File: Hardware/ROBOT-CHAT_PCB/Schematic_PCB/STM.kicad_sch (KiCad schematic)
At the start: 28 parts, among them J2 Conn_02x07_Odd_Even, J3 Conn_01x02, J4 Conn_01x02, SW1 SW_Push_Dual, U1 STM32WB55CEUx, Y1 32MHz

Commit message: Merge PCB v3
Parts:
- removed J2: Conn_02x07_Odd_Even, symbol Connector_Generic:Conn_02x07_Odd_Even
- removed Y1: 32MHz, XRCGB32M000F2P01R0:XRCGB32M000F2P01R0, symbol Device:Crystal_GND24_Small
- added J1: Conn_01x04, Connector_JST:JST_XH_B4B-XH-AM_1x04_P2.50mm_Vertical, symbol Connector_Generic:Conn_01x04
- added J201: Conn_ST_STDC14, Connector_PinHeader_1.27mm:PinHeader_2x07_P1.27mm_Vertical_SMD, symbol Connector:Conn_ST_STDC14
- added Y2: 32MHz, XRCGB32M000F2P01R0:XRCGB32M000F2P01R0, symbol Device:Crystal_GND24_Small
- added Y201: Crystal_Small, ABS07AIG-32.768KHZ-6-D-T:ABS07AIG-32.768KHZ-6-D-T, symbol Device:Crystal_Small
- C10, C13, C4, C5, C6, C7, C8: value 100nF -> 100n; footprint (none) -> Capacitor_SMD:C_0402_1005Metric
- C11, C15, C16, C3, C9: footprint (none) -> Capacitor_SMD:C_0603_1608Metric
- C12, C14, C17, C18: footprint (none) -> Capacitor_SMD:C_0402_1005Metric
- D1: footprint (none) -> LED_SMD:LED_0603_1608Metric
- J3, J4: footprint (none) -> Connector_JST:JST_PH_B2B-PH-K_1x02_P2.00mm_Vertical
- L1, L2: footprint (none) -> Inductor_SMD:L_0603_1608Metric
- R4, R5, R6: footprint (none) -> Resistor_SMD:R_0402_1005Metric
- SW1: footprint Button_Switch_SMD2:SW_Push_1P1T_NO_6x6mm_H9.5mm -> SW_Push_1P1T_NO_6x6mm_H9.5mm:SW_Push_1P1T_NO_6x6mm_H9.5mm
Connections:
- net +3.3V: now also C8.1, U1.40 (VDDUSB), J201.3 (VCC)
- net +5V: now also J1.4 (Pin_4); no longer C8.1, U1.40 (VDDUSB)
- net GND: now also J1.1 (Pin_1), J1.2 (Pin_2), J201.11 (GNDDetect), J201.5 (GND), J201.7 (GND), Y2.2, Y2.4
- net NRST: now also J201.12 (~{RST})
- net STATUS_LEDR: now also U1.13 (PA4); no longer U1.47 (PB7)
- net STATUS_LEDV: now also U1.12 (PA3); no longer U1.46 (PB6)
- net SWCLK: now also J201.6 (JCLK/SWCLK)
- net SWDIO: now also J201.4 (JTMS/SWDIO)
- net SWO: now also J201.8 (JTDO/SWO)
- net VCP_RX: now also U1.37 (PA11), J201.13 (VCP_RX); no longer U1.36 (PA10)
- net VCP_TX: now also U1.36 (PA10), J201.14 (VCP_TX); no longer U1.18 (PA9)
- net at C18.2, U1.3 (PC15): now also Y201.1
- net at C17.2, U1.2 (PC14): now also Y201.2
- net Encodeur_1B: now reaches U1.10 (PA1)
- net UART_TX: now reaches U1.11 (PA2)
- net UART_TX: now also J1.3 (Pin_3)
- net SCL: now reaches U1.14 (PA5)
- net REV_2: now reaches U1.15 (PA6)
- net FWD_2: now reaches U1.16 (PA7)
- net Encodeur_2A: now reaches U1.17 (PA8)
- net Antenne: now reaches U1.21 (RF1)
- net at U1.24 (OSC_OUT): now also Y2.3
- net at U1.25 (OSC_IN): now also Y2.1
- net INTacc1: now reaches U1.28 (PB0)
- net INTacc2: now reaches U1.29 (PB1)
- net SDA: now reaches U1.44 (PB4)
- net SCLacc: now reaches U1.5 (PB8)
- net SDAacc: now reaches U1.6 (PB9)
- net Encodeur_1A: now reaches U1.9 (PA0)
- net EN3.3: no longer names the net of U1.19 (PB2)
- net EN5: no longer names the net of U1.45 (PB5)
- net VFBSMPS: no longer names the net of C15.1, L2.2, U1.31 (VFBSMPS)
- net VLXSMPS: no longer names the net of L1.1, U1.33 (VLXSMPS)
- new net Encodeur_2B: U1.18 (PA9)
- new net FWD_1: U1.47 (PB7)
- new net REV_1: U1.46 (PB6)
- no-connect marks 4 -> 7
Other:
- note removed: "Faire le deuxième ocsillateur"
- moved on the sheet: C10, C11, C12, C13, C14, C15, C16, C17, C18, C3, C4, C5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

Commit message: Fixed error pins timers, PCB version 4
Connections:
- net FWD_1: now also U1.15 (PA6); no longer U1.47 (PB7)
- net REV_2: now also U1.47 (PB7); no longer U1.15 (PA6)
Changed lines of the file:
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@@
 	(hierarchical_label "FWD_1"
 		(shape input)
-		(at 177.8 135.89 0)
+		(at 177.8 90.17 0)
 		(effects
 			(font
@@
 	(hierarchical_label "REV_2"
 		(shape input)
-		(at 177.8 90.17 0)
+		(at 177.8 135.89 0)
 		(effects
 			(font

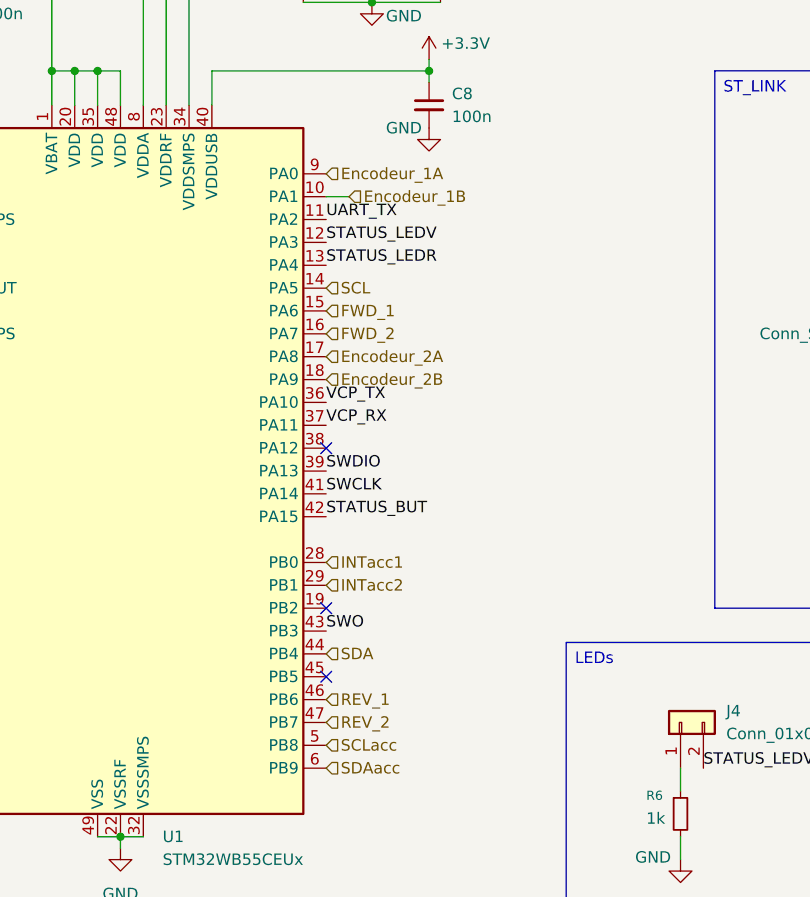
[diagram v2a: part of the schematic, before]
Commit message: Modif PCB after pin update, PCB version 5
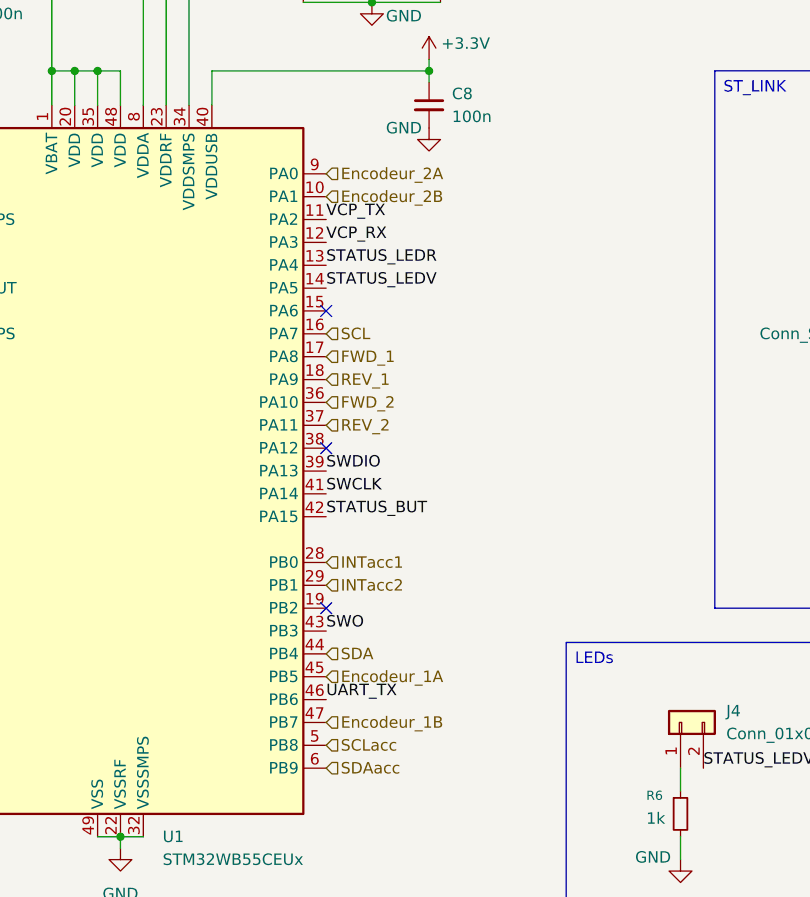
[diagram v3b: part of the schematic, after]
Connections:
- net Encodeur_1A: now also U1.45 (PB5); no longer U1.9 (PA0)
- net Encodeur_1B: now also U1.47 (PB7); no longer U1.10 (PA1)
- net Encodeur_2A: now also U1.9 (PA0); no longer U1.17 (PA8)
- net Encodeur_2B: now also U1.10 (PA1); no longer U1.18 (PA9)
- net FWD_1: now also U1.17 (PA8); no longer U1.15 (PA6)
- net FWD_2: now also U1.36 (PA10); no longer U1.16 (PA7)
- net REV_1: now also U1.18 (PA9); no longer U1.46 (PB6)
- net REV_2: now also U1.37 (PA11); no longer U1.47 (PB7)
- net SCL: now also U1.16 (PA7); no longer U1.14 (PA5)
- net STATUS_LEDV: now also U1.14 (PA5); no longer U1.12 (PA3)
- net UART_TX: now also U1.46 (PB6); no longer U1.11 (PA2)
- net VCP_RX: now also U1.12 (PA3); no longer U1.37 (PA11)
- net VCP_TX: now also U1.11 (PA2); no longer U1.36 (PA10)
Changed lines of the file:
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@@
 	)
 	(no_connect
-		(at 177.8 130.81)
+		(at 177.8 90.17)
 	)
 	(no_connect
@@
 	(wire
 		(pts
-			(xy 180.34 77.47) (xy 177.8 77.47)
-		)
-		(stroke
-			(width 0)
-			(type default)
-		)
-	)
-	(wire
-		(pts
 			(xy 189.23 62.23) (xy 189.23 63.5)
 		)
@@
 		)
 	)
-	(label "VCP_RX"
-		(at 177.8 102.87 0)
+	(label "STATUS_LEDV"
+		(at 177.8 87.63 0)
 		(effects
 			(font
@@
 		)
 	)
+	(label "VCP_RX"
+		(at 177.8 82.55 0)
+		(effects
+			(font
+				(size 1.27 1.27)
+			)
+			(justify left bottom)
+		)
+	)
 	(label "VCP_TX"
-		(at 177.8 100.33 0)
+		(at 177.8 80.01 0)
+		(effects
+			(font
+				(size 1.27 1.27)
+			)
+			(justify left bottom)
+		)
+	)
+	(label "UART_TX"
+		(at 177.8 133.35 0)
 		(effects
 			(font
@@
 		)
 	)
-	(label "STATUS_LEDV"
-		(at 177.8 82.55 0)
-		(effects
-			(font
-				(size 1.27 1.27)
-			)
-			(justify left bottom)
-		)
-	)
-	(label "UART_TX"
-		(at 177.8 80.01 0)
-		(effects
-			(font
-				(size 1.27 1.27)
-			)
-			(justify left bottom)
+	(hierarchical_label "Encodeur_1A"
+		(shape input)
+		(at 177.8 130.81 0)
+		(effects
+			(font
+				(size 1.27 1.27)
+			)
+			(justify left)
+		)
+	)
+	(hierarchical_label "FWD_1"
+		(shape input)
+		(at 177.8 95.25 0)
+		(effects
+			(font
+				(size 1.27 1.27)
+			)
+			(justify left)
+		)
+	)
+	(hierarchical_label "REV_1"
+		(shape input)
+		(at 177.8 97.79 0)
+		(effects
+			(font
+				(size 1.27 1.27)
+			)
+			(justify left)
+		)
+	)
+	(hierarchical_label "SDAacc"
+		(shape input)
+		(at 177.8 140.97 0)
+		(effects
+			(font
+				(size 1.27 1.27)
+			)
+			(justify left)
+		)
+	)
+	(hierarchical_label "INTacc2"
+		(shape input)
+		(at 177.8 120.65 0)
+		(effects
+			(font
+				(size 1.27 1.27)
+			)
+			(justify left)
+		)
+	)
+	(hierarchical_label "Antenne"
+		(shape input)
+		(at 132.08 97.79 180)
+		(effects
+			(font
+				(size 1.27 1.27)
+			)
+			(justify right)
+		)
+	)
+	(hierarchical_label "SCLacc"
+		(shape input)
+		(at 177.8 138.43 0)
+		(effects
+			(font
+				(size 1.27 1.27)
+			)
+			(justify left)
+		)
+	)
+	(hierarchical_label "INTacc1"
+		(shape input)
+		(at 177.8 118.11 0)
+		(effects
+			(font
+				(size 1.27 1.27)
+			)
+			(justify left)
+		)
+	)
+	(hierarchical_label "Encodeur_1B"
+		(shape input)
+		(at 177.8 135.89 0)
+		(effects
+			(font
+				(size 1.27 1.27)
+			)
+			(justify left)
+		)
+	)
+	(hierarchical_label "Encodeur_2B"
+		(shape input)
+		(at 177.8 77.47 0)
+		(effects
+			(font
+				(size 1.27 1.27)
+			)
+			(justify left)
+		)
+	)
+	(hierarchical_label "SCL"
+		(shape input)
+		(at 177.8 92.71 0)
+		(effects
+			(font
+				(size 1.27 1.27)
+			)
+			(justify left)
+		)
+	)
+	(hierarchical_label "REV_2"
+		(shape input)
+		(at 177.8 102.87 0)
+		(effects
+			(font
+				(size 1.27 1.27)
+			)
+			(justify left)
+		)
+	)
+	(hierarchical_label "SDA"
+		(shape input)
+		(at 177.8 128.27 0)
+		(effects
+			(font
+				(size 1.27 1.27)
+			)
+			(justify left)
+		)
+	)
+	(hierarchical_label "Encodeur_2A"
+		(shape input)
+		(at 177.8 74.93 0)
+		(effects
+			(font
+				(size 1.27 1.27)
+			)
+			(justify left)
 		)
 	)
 	(hierarchical_label "FWD_2"
 		(shape input)
-		(at 177.8 92.71 0)
-		(effects
-			(font
-				(size 1.27 1.27)
-			)
-			(justify left)
-		)
-	)
-	(hierarchical_label "Encodeur_1A"
-		(shape input)
-		(at 177.8 74.93 0)
-		(effects
-			(font
-				(size 1.27 1.27)
-			)
-			(justify left)
-		)
-	)
-	(hierarchical_label "REV_1"
-		(shape input)
-		(at 177.8 133.35 0)
-		(effects
-			(font
-				(size 1.27 1.27)
-			)
-			(justify left)
-		)
-	)
-	(hierarchical_label "Encodeur_2B"
-		(shape input)
-		(at 177.8 97.79 0)
-		(effects
-			(font
-				(size 1.27 1.27)
-			)
-			(justify left)
-		)
-	)
-	(hierarchical_label "FWD_1"
-		(shape input)
-		(at 177.8 90.17 0)
-		(effects
-			(font
-				(size 1.27 1.27)
-			)
-			(justify left)
-		)
-	)
-	(hierarchical_label "SDAacc"
-		(shape input)
-		(at 177.8 140.97 0)
-		(effects
-			(font
-				(size 1.27 1.27)
-			)
-			(justify left)
-		)
-	)
-	(hierarchical_label "INTacc2"
-		(shape input)
-		(at 177.8 120.65 0)
-		(effects
-			(font
-				(size 1.27 1.27)
-			)
-			(justify left)
-		)
-	)
-	(hierarchical_label "Antenne"
-		(shape input)
-		(at 132.08 97.79 180)
-		(effects
-			(font
-				(size 1.27 1.27)
-			)
-			(justify right)
-		)
-	)
-	(hierarchical_label "Encodeur_2A"
-		(shape input)
-		(at 177.8 95.25 0)
-		(effects
-			(font
-				(size 1.27 1.27)
-			)
-			(justify left)
-		)
-	)
-	(hierarchical_label "SCLacc"
-		(shape input)
-		(at 177.8 138.43 0)
-		(effects
-			(font
-				(size 1.27 1.27)
-			)
-			(justify left)
-		)
-	)
-	(hierarchical_label "REV_2"
-		(shape input)
-		(at 177.8 135.89 0)
-		(effects
-			(font
-				(size 1.27 1.27)
-			)
-			(justify left)
-		)
-	)
-	(hierarchical_label "INTacc1"
-		(shape input)
-		(at 177.8 118.11 0)
-		(effects
-			(font
-				(size 1.27 1.27)
-			)
-			(justify left)
-		)
-	)
-	(hierarchical_label "Encodeur_1B"
-		(shape input)
-		(at 180.34 77.47 0)
-		(effects
-			(font
-				(size 1.27 1.27)
-			)
-			(justify left)
-		)
-	)
-	(hierarchical_label "SCL"
-		(shape input)
-		(at 177.8 87.63 0)
-		(effects
-			(font
-				(size 1.27 1.27)
-			)
-			(justify left)
-		)
-	)
-	(hierarchical_label "SDA"
-		(shape input)
-		(at 177.8 128.27 0)
-		(effects
-			(font
+		(at 177.8 100.33 0)
+		(effects
+			(font

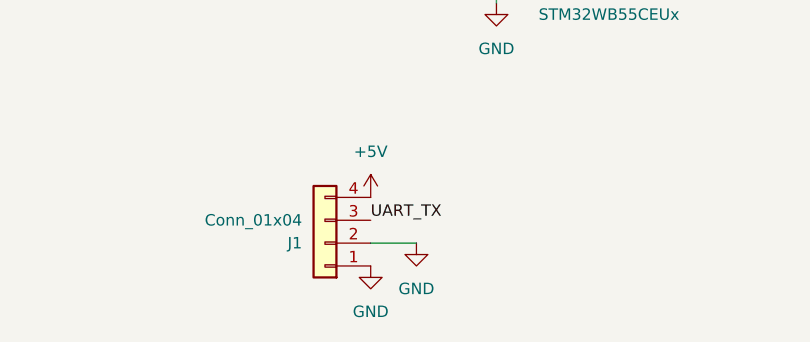
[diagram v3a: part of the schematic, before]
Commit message: Modified pin M_control for the Lidar, PCV version 7
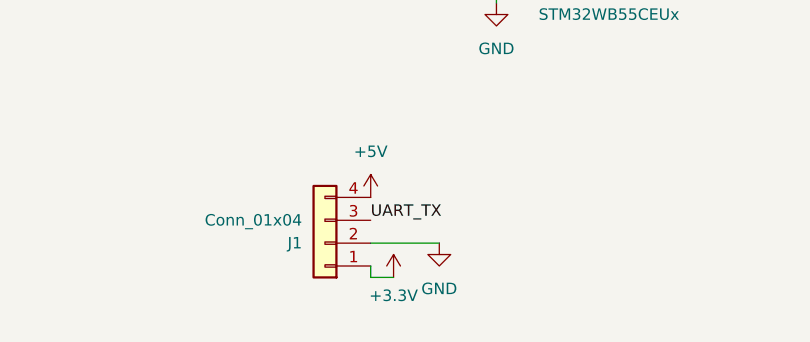
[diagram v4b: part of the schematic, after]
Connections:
- net +3.3V: now also J1.1 (Pin_1)
- net GND: no longer J1.1 (Pin_1)
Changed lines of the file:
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@@
 	(wire
 		(pts
-			(xy 146.05 176.53) (xy 140.97 176.53)
+			(xy 148.59 176.53) (xy 140.97 176.53)
 		)
 		(stroke
@@
 	(wire
 		(pts
+			(xy 140.97 179.07) (xy 140.97 180.34)
+		)
+		(stroke
+			(width 0)
+			(type default)
+		)
+	)
+	(wire
+		(pts
 			(xy 182.88 55.88) (xy 190.5 55.88)
 		)
@@
 	(wire
 		(pts
+			(xy 140.97 180.34) (xy 143.51 180.34)
+		)
+		(stroke
+			(width 0)
+			(type default)
+		)
+	)
+	(wire
+		(pts
 			(xy 93.98 120.65) (xy 93.98 123.19)
 		)
@@
 	(symbol
 		(lib_id "power:GND")
-		(at 140.97 179.07 0)
-		(unit 1)
-		(exclude_from_sim no)
-		(in_bom yes)
-		(on_board yes)
-		(dnp no)
-		(fields_autoplaced yes)
-		(property "Reference" "#PWR055"
-			(at 140.97 185.42 0)
-			(effects
-				(font
-					(size 1.27 1.27)
-				)
-				(hide yes)
-			)
-		)
-		(property "Value" "GND"
-			(at 140.97 184.15 0)
-			(effects
-				(font
-					(size 1.27 1.27)
-				)
-			)
-		)
-		(property "Footprint" ""
-			(at 140.97 179.07 0)
-			(effects
-				(font
-					(size 1.27 1.27)
-				)
-				(hide yes)
-			)
-		)
-		(property "Datasheet" ""
-			(at 140.97 179.07 0)
-			(effects
-				(font
-					(size 1.27 1.27)
-				)
-				(hide yes)
-			)
-		)
-		(property "Description" "Power symbol creates a global label with name \"GND\" , ground"
-			(at 140.97 179.07 0)
-			(effects
-				(font
-					(size 1.27 1.27)
-				)
-				(hide yes)
-			)
-		)
-		(pin "1"
-		)
-		(instances
-			(project "PCB_robot_chat"
-				(path "/3534a4da-1897-4a3c-809d-843e7f41fadb/6dd21f76-e181-4380-95ef-cbdd4cbc38f9"
-					(reference "#PWR055")
-					(unit 1)
-				)
-			)
-		)
-	)
-	(symbol
-		(lib_id "power:GND")
-		(at 146.05 176.53 0)
+		(at 148.59 176.53 0)
 		(unit 1)
 		(exclude_from_sim no)
@@
 		(fields_autoplaced yes)
 		(property "Reference" "#PWR056"
-			(at 146.05 182.88 0)
+			(at 148.59 182.88 0)
 			(effects
 				(font
@@
 		)
 		(property "Value" "GND"
-			(at 146.05 181.61 0)
+			(at 148.59 181.61 0)
 			(effects
 				(font
@@
 		)
 		(property "Footprint" ""
-			(at 146.05 176.53 0)
+			(at 148.59 176.53 0)
 			(effects
 				(font
@@
 		)
 		(property "Datasheet" ""
-			(at 146.05 176.53 0)
+			(at 148.59 176.53 0)
 			(effects
 				(font
@@
 		)
 		(property "Description" "Power symbol creates a global label with name \"GND\" , ground"
-			(at 146.05 176.53 0)
+			(at 148.59 176.53 0)
 			(effects
 				(font
@@
 					(unit 1)
 				)
+			)
+		)
+	)
+	(symbol
+		(lib_id "power:+3.3V")
+		(at 143.51 180.34 0)
+		(unit 1)
+		(exclude_from_sim no)
+		(in_bom yes)
+		(on_board yes)
+		(dnp no)
+		(property "Reference" "#PWR0202"
+			(at 143.51 184.15 0)
+			(effects
+				(font
+					(size 1.27 1.27)
+				)
+				(hide yes)
+			)
+		)
+		(property "Value" "+3.3V"
+			(at 143.51 182.372 0)
+			(effects
+				(font
+					(size 1.27 1.27)
+				)
+			)
+		)
+		(property "Footprint" ""
+			(at 143.51 180.34 0)
+			(effects
+				(font
+					(size 1.27 1.27)
+				)
+				(hide yes)
+			)
+		)
+		(property "Datasheet" ""
+			(at 143.51 180.34 0)
+			(effects
+				(font
+					(size 1.27 1.27)
+				)
+				(hide yes)
+			)
+		)
+		(property "Description" "Power symbol creates a global label with name \"+3.3V\""
+			(at 143.51 180.34 0)
+			(effects
+				(font
+					(size 1.27 1.27)
+				)
+				(hide yes)
+			)
+		)
+		(pin "1"
+		)
+		(instances
+			(project ""
+				(path "/3534a4da-1897-4a3c-809d-843e7f41fadb/6dd21f76-e181-4380-95ef-cbdd4cbc38f9"
+					(reference "#PWR0202")
+					(unit 1)
+				)
